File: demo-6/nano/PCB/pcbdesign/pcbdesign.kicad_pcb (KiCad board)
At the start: 2 copper layers, 5 parts, among them J1 Conn_01x15_Female, J2 Conn_01x15_Female

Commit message: ready for pcb
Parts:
- added C1: 100 mF, Capacitor_THT:CP_Radial_D8.0mm_P3.50mm, F.Cu at (54.6, 35.6)
- added D2: 5V, Diode_THT:D_A-405_P7.62mm_Horizontal, F.Cu at (71.1, 43.2)
- added F1: 1.6A Fuse, Fuse:Fuseholder_Cylinder-6.3x32mm_Schurter_0031-8002_Horizontal_Open, F.Cu at (35.6, 53.3)
- added F2: 250ma Fuse, Fuse:Fuseholder_Cylinder-6.3x32mm_Schurter_0031-8002_Horizontal_Open, F.Cu at (85.1, 21.6)
- added J3: Encoder, Connector_PinSocket_2.54mm:PinSocket_1x05_P2.54mm_Vertical, F.Cu at (83.8, 86.4)
- added J4: HC-SR04, Connector_PinSocket_2.54mm:PinSocket_1x04_P2.54mm_Vertical, F.Cu at (17.8, 86.4)
- added J5: Display, Connector_PinSocket_2.54mm:PinSocket_1x04_P2.54mm_Vertical, F.Cu at (83.8, 69.8)
- added J6: Inflow Relay, TerminalBlock:TerminalBlock_bornier-2_P5.08mm, F.Cu at (19.1, 64.8)
- added J7: Outflow Switch, TerminalBlock:TerminalBlock_bornier-2_P5.08mm, F.Cu at (19.1, 41.9)
- added J8: Outflow Pump, TerminalBlock:TerminalBlock_bornier-2_P5.08mm, F.Cu at (19.1, 53.3)
- added PS1: RY-1205S, RY-1205S:CONV_RY-1205S, F.Cu at (76.2, 35.6)
- added Q1: PN2222A, Package_TO_SOT_THT:TO-92_Inline, F.Cu at (22.9, 76.2)
- added R2: 220, Resistor_THT:R_Axial_DIN0207_L6.3mm_D2.5mm_P7.62mm_Horizontal, F.Cu at (35.6, 77.5)
- added R3: 10K, Resistor_THT:R_Axial_DIN0207_L6.3mm_D2.5mm_P7.62mm_Horizontal, F.Cu at (78.7, 87.6)
- added R4: 10K, Resistor_THT:R_Axial_DIN0207_L6.3mm_D2.5mm_P7.62mm_Horizontal, F.Cu at (35.6, 82.5)
- D1: footprint LED_THT:LED_D3.0mm -> LED_THT:LED_D4.0mm
- J1: value Conn_01x15_Female -> Relay; footprint Connector_PinSocket_2.54mm:PinSocket_1x15_P2.54mm_Vertical -> Connector_PinSocket_2.54mm:PinSocket_1x03_P2.54mm_Vertical
- J2: value Conn_01x15_Female -> 12v input; footprint Connector_PinSocket_2.54mm:PinSocket_1x15_P2.54mm_Vertical -> Connector_BarrelJack:BarrelJack_CUI_PJ-063AH_Horizontal
- R1: footprint Resistor_THT:R_Axial_DIN0204_L3.6mm_D1.6mm_P5.08mm_Horizontal -> Resistor_THT:R_Axial_DIN0207_L6.3mm_D2.5mm_P7.62mm_Horizontal
- moved J2 160.8 mm to (25.4, 19.1), turned to 270 degrees
- moved J1 98.6 mm to (16.5, 73.7), turned to 0 degrees
- moved R1 79.0 mm to (27.9, 73.7), turned to 0 degrees
- moved D1 75.7 mm to (29.2, 63.5), turned to 0 degrees
- moved A1 73.3 mm to (47.0, 49.5)
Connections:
- A1 pad 1: Net-(A1-Pad1) -> (no net)
- A1 pad 10: Net-(A1-Pad10) -> (no net)
- A1 pad 11: Net-(A1-Pad11) -> (no net)
- A1 pad 12: Net-(A1-Pad12) -> (no net)
- A1 pad 15: Net-(A1-Pad15) -> (no net)
- A1 pad 16: Net-(A1-Pad16) -> (no net)
- A1 pad 17: Net-(A1-Pad17) -> (no net)
- A1 pad 18: Net-(A1-Pad18) -> (no net)
- A1 pad 19: Net-(A1-Pad19) -> (no net)
- A1 pad 2: Net-(A1-Pad2) -> (no net)
- A1 pad 20: Net-(A1-Pad20) -> (no net)
- A1 pad 21: Net-(A1-Pad21) -> (no net)
- A1 pad 22: Net-(A1-Pad22) -> (no net)
- A1 pad 25: Net-(A1-Pad25) -> (no net)
- A1 pad 26: Net-(A1-Pad26) -> (no net)
- A1 pad 27: +1V5 -> +5V
- A1 pad 28: Net-(A1-Pad28) -> (no net)
- A1 pad 3: Net-(A1-Pad3) -> (no net)
- A1 pad 30: Net-(A1-Pad30) -> (no net)
- A1 pad 9: Net-(A1-Pad9) -> (no net)
- D1 pad 1: GND -> Net-(D1-Pad1)
- D1 pad 2: Net-(D1-Pad2) -> Net-(A1-Pad8)
- J1 pad 1: Net-(A1-Pad16) -> +5V
- J1 pad 2: Net-(A1-Pad15) -> GND
- J1 pad 3: Net-(A1-Pad14) -> Net-(J1-Pad3)
- J2 pad 2: Net-(A1-Pad28) -> Net-(J2-Pad2)
- R1 pad 1: Net-(A1-Pad13) -> Net-(Q1-Pad1)
- R1 pad 2: Net-(D1-Pad2) -> GND
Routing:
- net Net-(A1-Pad3): track 107.1 -> 0.00 mm
- net Net-(A1-Pad28): track 50.9 -> 0.00 mm
- net Net-(A1-Pad16): track 27.5 -> 0.00 mm
- net Net-(A1-Pad1): track 23.6 -> 0.00 mm
- net GND: track 21.1 -> 0.00 mm, vias 2 -> 0
- net Net-(A1-Pad13): track 16.2 -> 0.00 mm
- net Net-(A1-Pad18): track 13.0 -> 0.00 mm
- net Net-(A1-Pad26): track 12.0 -> 0.00 mm
- net Net-(A1-Pad25): track 12.0 -> 0.00 mm
- net Net-(A1-Pad24): track 12.0 -> 0.00 mm
- net Net-(A1-Pad23): track 12.0 -> 0.00 mm
- net Net-(A1-Pad22): track 12.0 -> 0.00 mm
- net Net-(A1-Pad21): track 12.0 -> 0.00 mm
- net Net-(A1-Pad19): track 12.0 -> 0.00 mm
- net Net-(A1-Pad20): track 12.0 -> 0.00 mm
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- removed copper zone on F.Cu, net GND
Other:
- board text removed: "CRGAR"

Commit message: pcb ready
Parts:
- moved A1 110.2 mm to (146.1, 97.8)
- moved D1 110.2 mm to (128.3, 111.8)
- moved D2 110.2 mm to (170.2, 91.4)
- moved J2 110.2 mm to (124.5, 67.3)
- moved J3 110.2 mm to (182.9, 134.6)
- moved J4 110.2 mm to (116.8, 134.6)
- moved J5 110.2 mm to (182.9, 118.1)
- moved J6 110.2 mm to (118.1, 113.0)
- moved J7 110.2 mm to (118.1, 90.2)
- moved R1 110.2 mm to (127.0, 121.9)
- moved R2 110.2 mm to (134.6, 125.7)
- moved R3 110.2 mm to (177.8, 135.9)
- moved R4 110.2 mm to (134.6, 130.8)
- moved C1 110.2 mm to (153.7, 83.8)
- moved F1 110.2 mm to (134.6, 101.6)
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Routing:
- net +5V: track 0.00 -> 153.6 mm
- net Net-(J2-Pad2): track 0.00 -> 127.3 mm
- net Net-(F1-Pad1): track 0.00 -> 83.5 mm
- net Net-(A1-Pad6): track 0.00 -> 70.5 mm
- net Net-(A1-Pad5): track 0.00 -> 69.9 mm
- net Net-(A1-Pad7): track 0.00 -> 68.1 mm
- net Net-(A1-Pad14): track 0.00 -> 27.0 mm
- net GND: track 0.00 -> 24.3 mm, vias 0 -> 1
- net Net-(A1-Pad13): track 0.00 -> 24.2 mm
- net Net-(C1-Pad1): track 0.00 -> 23.1 mm
- net Net-(A1-Pad24): track 0.00 -> 22.6 mm
- net Net-(A1-Pad23): track 0.00 -> 22.6 mm
- net Net-(D1-Pad1): track 0.00 -> 21.7 mm
- net Net-(A1-Pad8): track 0.00 -> 16.8 mm
- net Net-(F2-Pad1): track 0.00 -> 16.7 mm
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- added copper zone on F.Cu, net GND

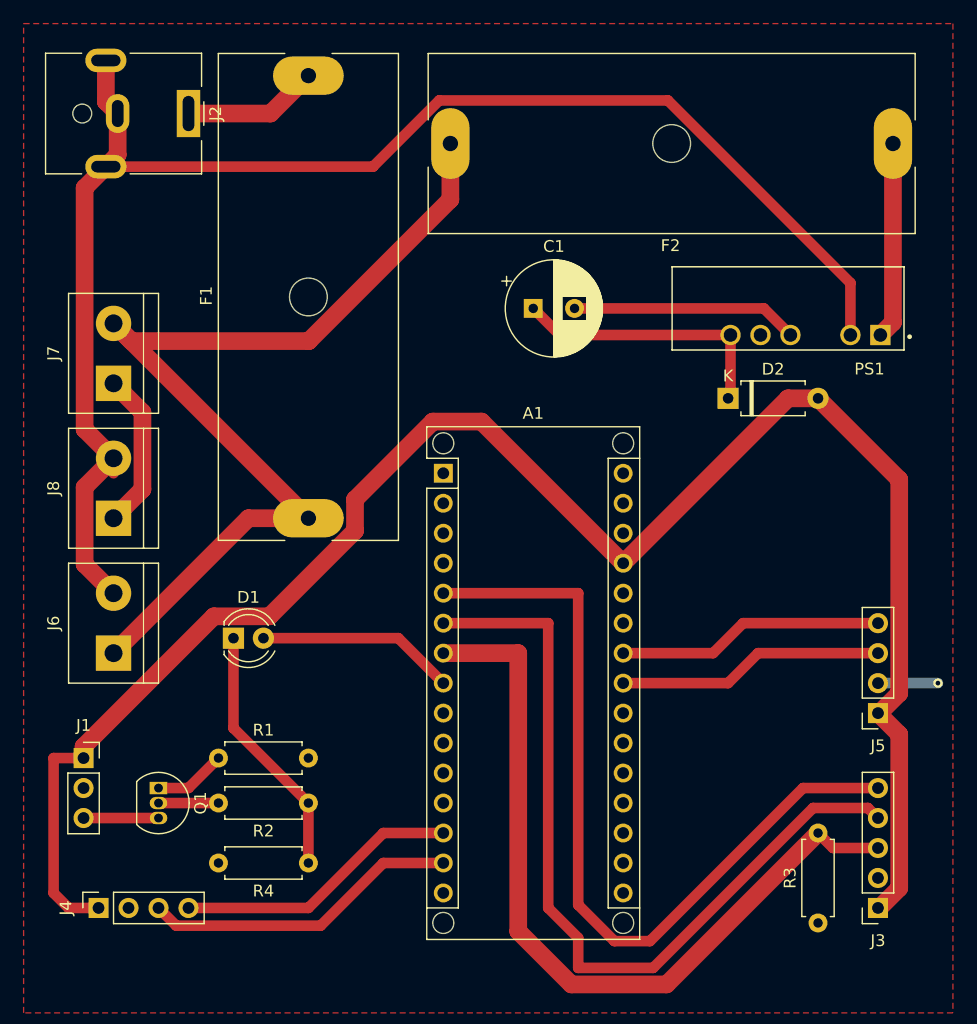
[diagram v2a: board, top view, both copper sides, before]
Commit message: adding labels
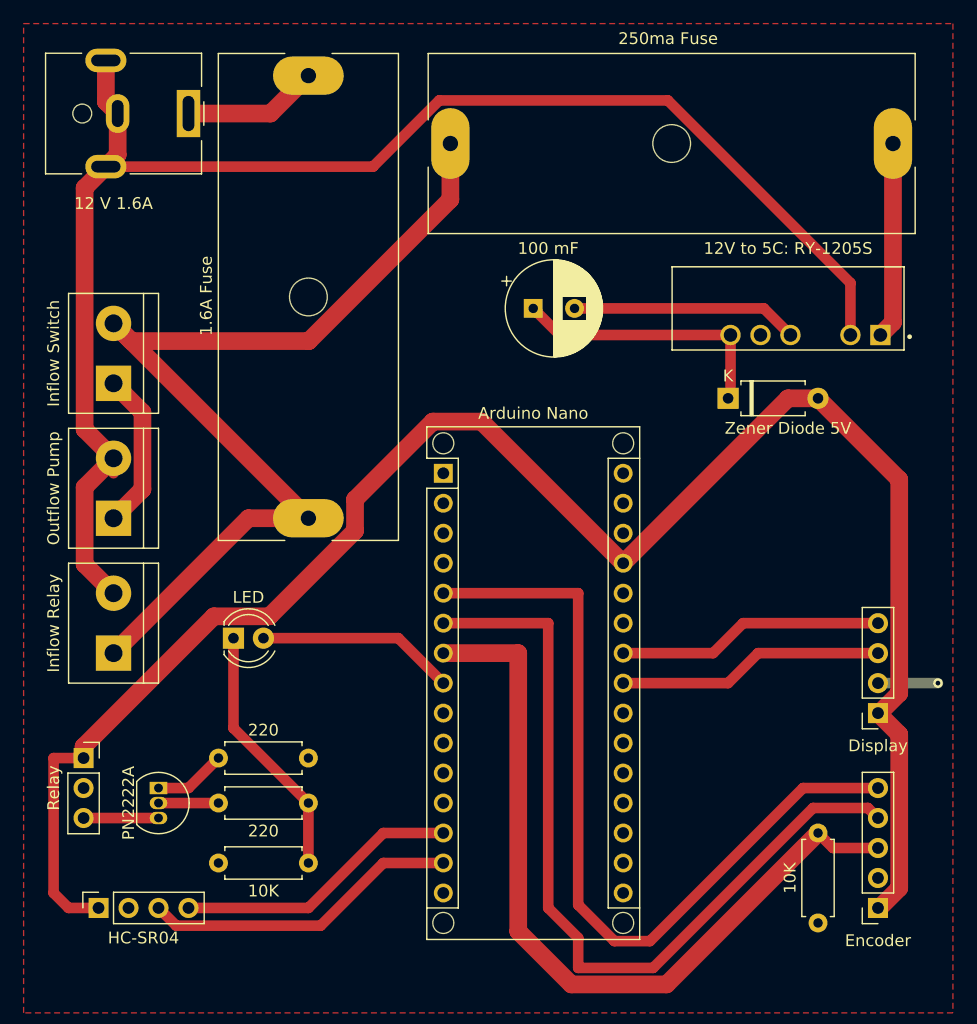
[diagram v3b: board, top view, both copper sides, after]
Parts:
- 1.6A Fuse: renamed from F1
- 100 mF: renamed from C1
- 12 V 1.6A: renamed from J2
- 12V to 5C: RY-1205S: renamed from PS1
- 250ma Fuse: renamed from F2
- Arduino Nano: renamed from A1
- Inflow Relay: renamed from J6
- Inflow Switch: renamed from J7
- Outflow Pump: renamed from J8
- Zener Diode 5V: renamed from D2
- renumbered R4 to 10K, R3 to 10K, R2 to 220, R1 to 220, J5 to Display, J3 to Encoder, J4 to HC-SR04, D1 to LED, Q1 to PN2222A, J1 to Relay
